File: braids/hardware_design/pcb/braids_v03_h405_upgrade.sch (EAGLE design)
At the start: 95 parts, among them IC1 74HC595D, IC2 74HC595D, IC3 LM4040B25, IC4 LM4040B10, IC5 DAC8551, IC6 LM1117-5.0, IC8 MCP6004, IC9 TL072, Q1 MMBT3904, Q2 MMBT3904, Q3 MMBT3904, Q4 MMBT3904, Q6 MMBT3904, SW1 EC12E_SW

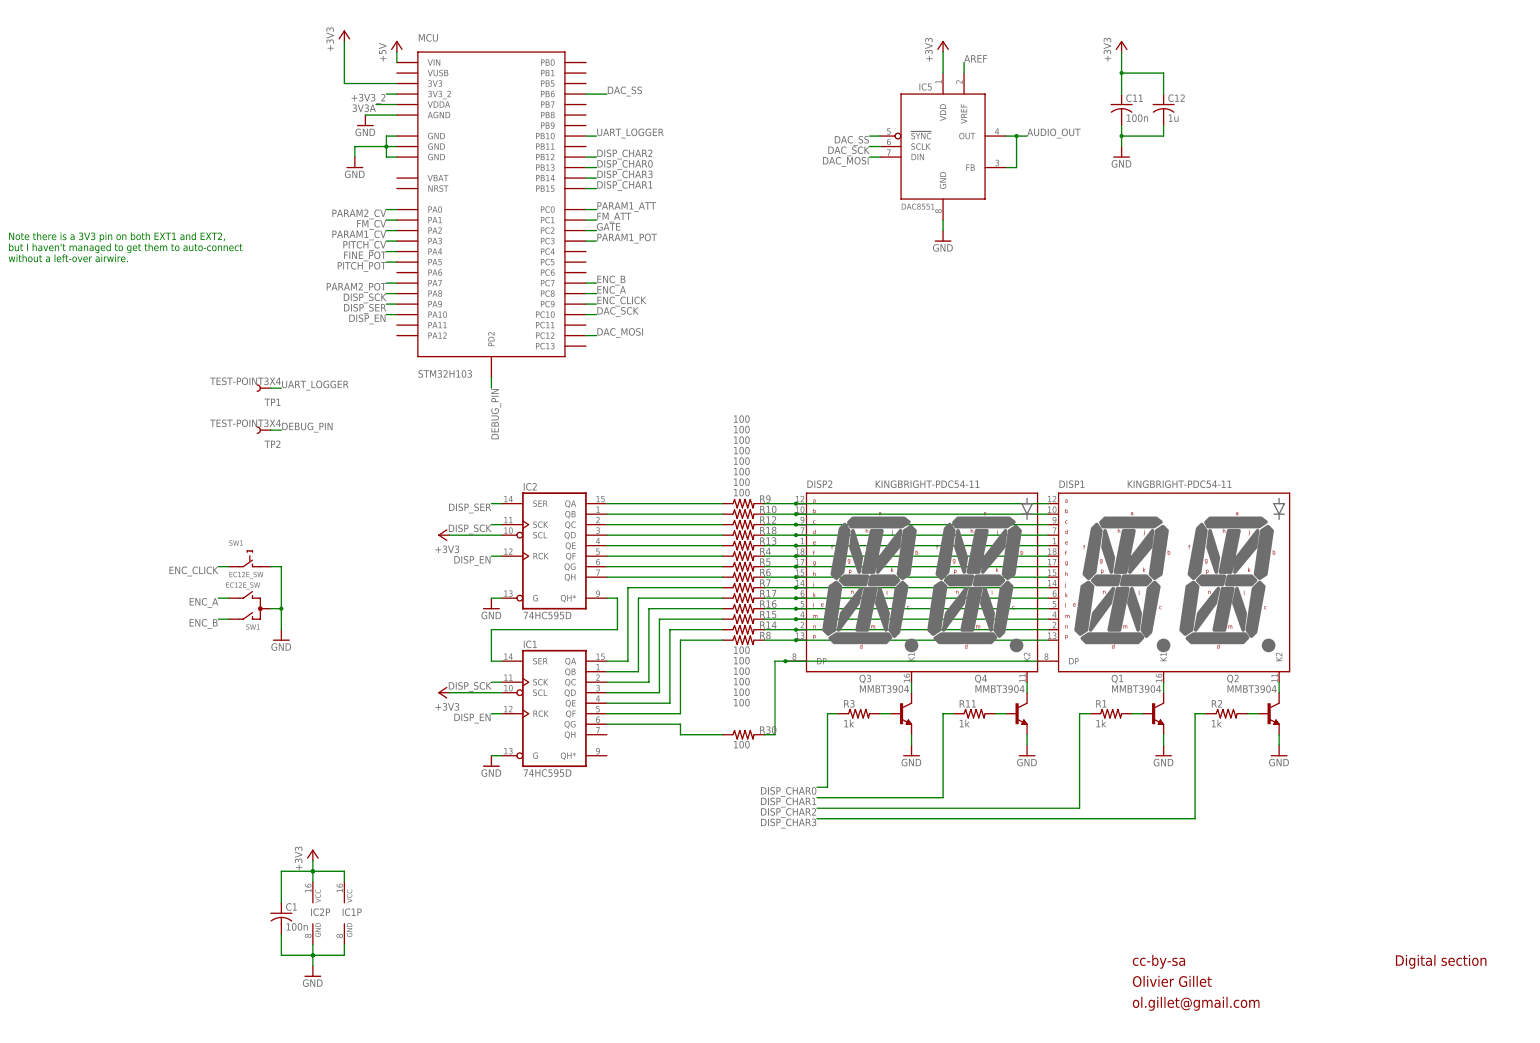
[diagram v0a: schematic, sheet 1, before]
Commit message: Add switches and LEDs, DAC uses +3V3_A
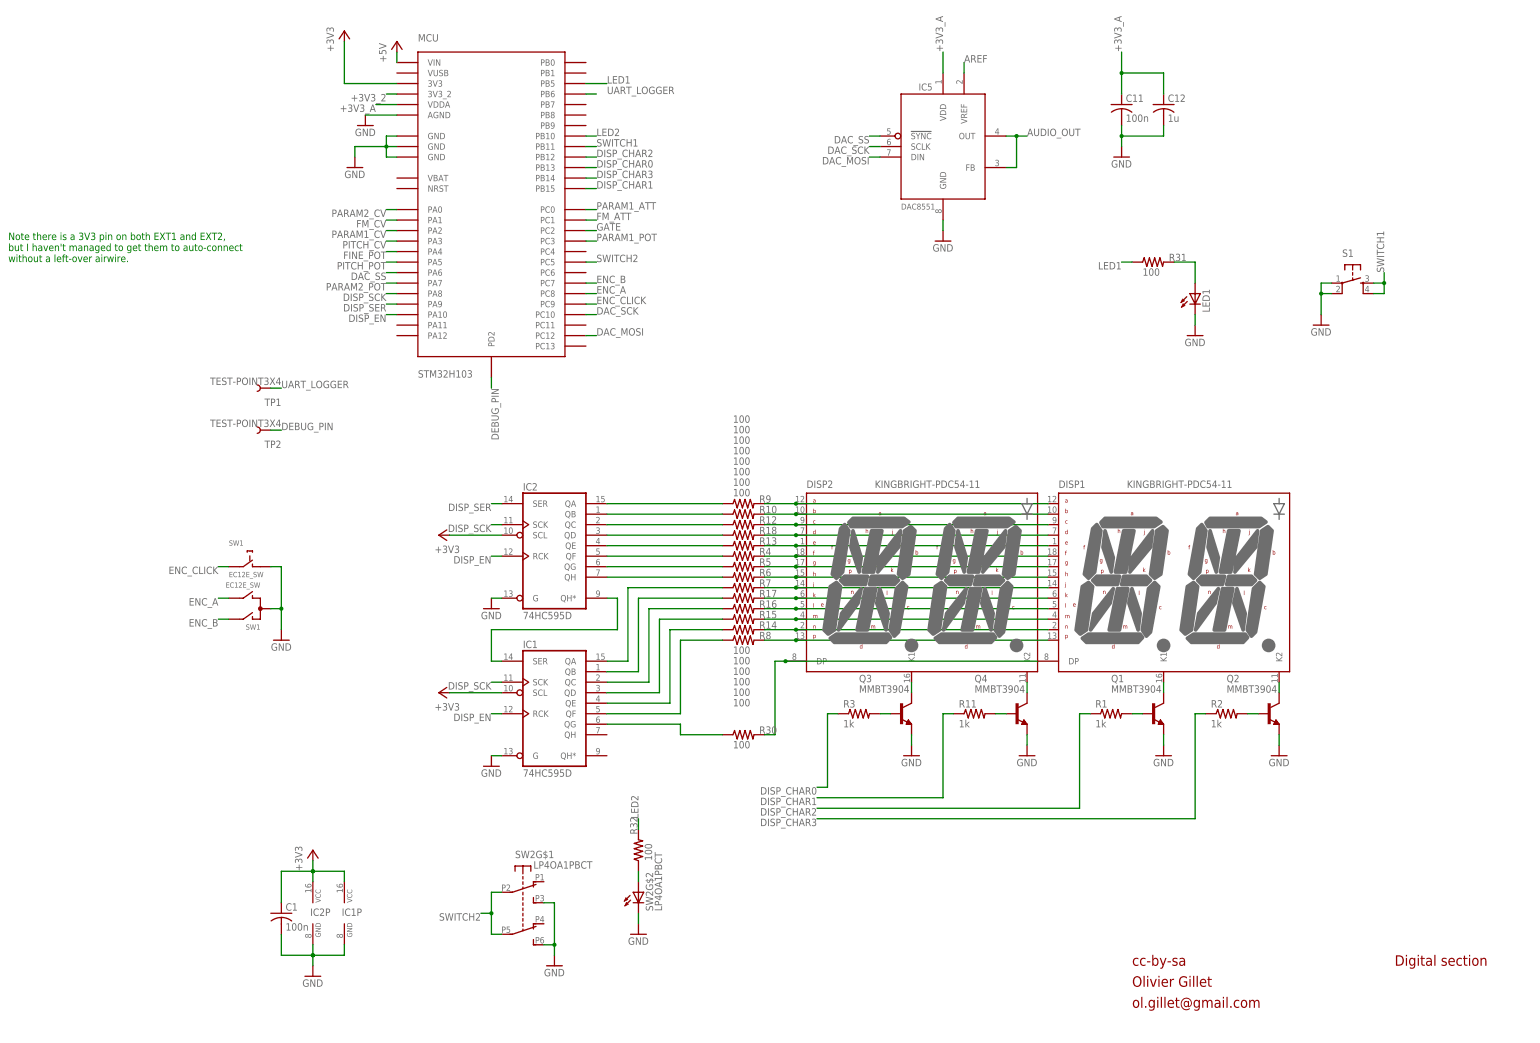
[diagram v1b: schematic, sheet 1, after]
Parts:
- added LED1: (no value), led:LED3MM
- added R31, R32: 100, rcl:R-US_R0603
- added S1: (no value), SparkFun:TAC_SWITCHPTH
- added SW2: LP4OA1PBCT, og-switch:LP4OA1PBCT
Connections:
- removed net 3V3A: C18.1, IC8P.V+, MCU.VDDA, R19.E, R20.E, R21.E, R22.1, R35.E, R36.E, R37.E
- new net +3V3_A: C11.1, C12.1, C18.1, IC5.VDD, IC8P.V+, MCU.VDDA, R19.E, R20.E, R21.E, R22.1, R35.E, R36.E, R37.E
- new net LED1: MCU.PB5, R31.1
- new net LED2: MCU.PB10, R32.2
- new net N$47: LED1.A, R31.2
- new net N$48: R32.1, SW2G$2.L1
- new net SWITCH1: MCU.PB11, S1.3, S1.4
- new net SWITCH2: MCU.PC5, SW2G$1.A2, SW2G$1.B2
- net +3V3: no longer C11.1, C12.1, IC5.VDD
- net DAC_SS: now also MCU.PA6; no longer MCU.PB6
- net GND: now also LED1.C, S1.1, S1.2, SW2G$1.A3, SW2G$1.B3, SW2G$2.L2
- net UART_LOGGER: now also MCU.PB6; no longer MCU.PB10

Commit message: Re-assign some GPIOs due to conflicts on Olimex boards, some tweaks
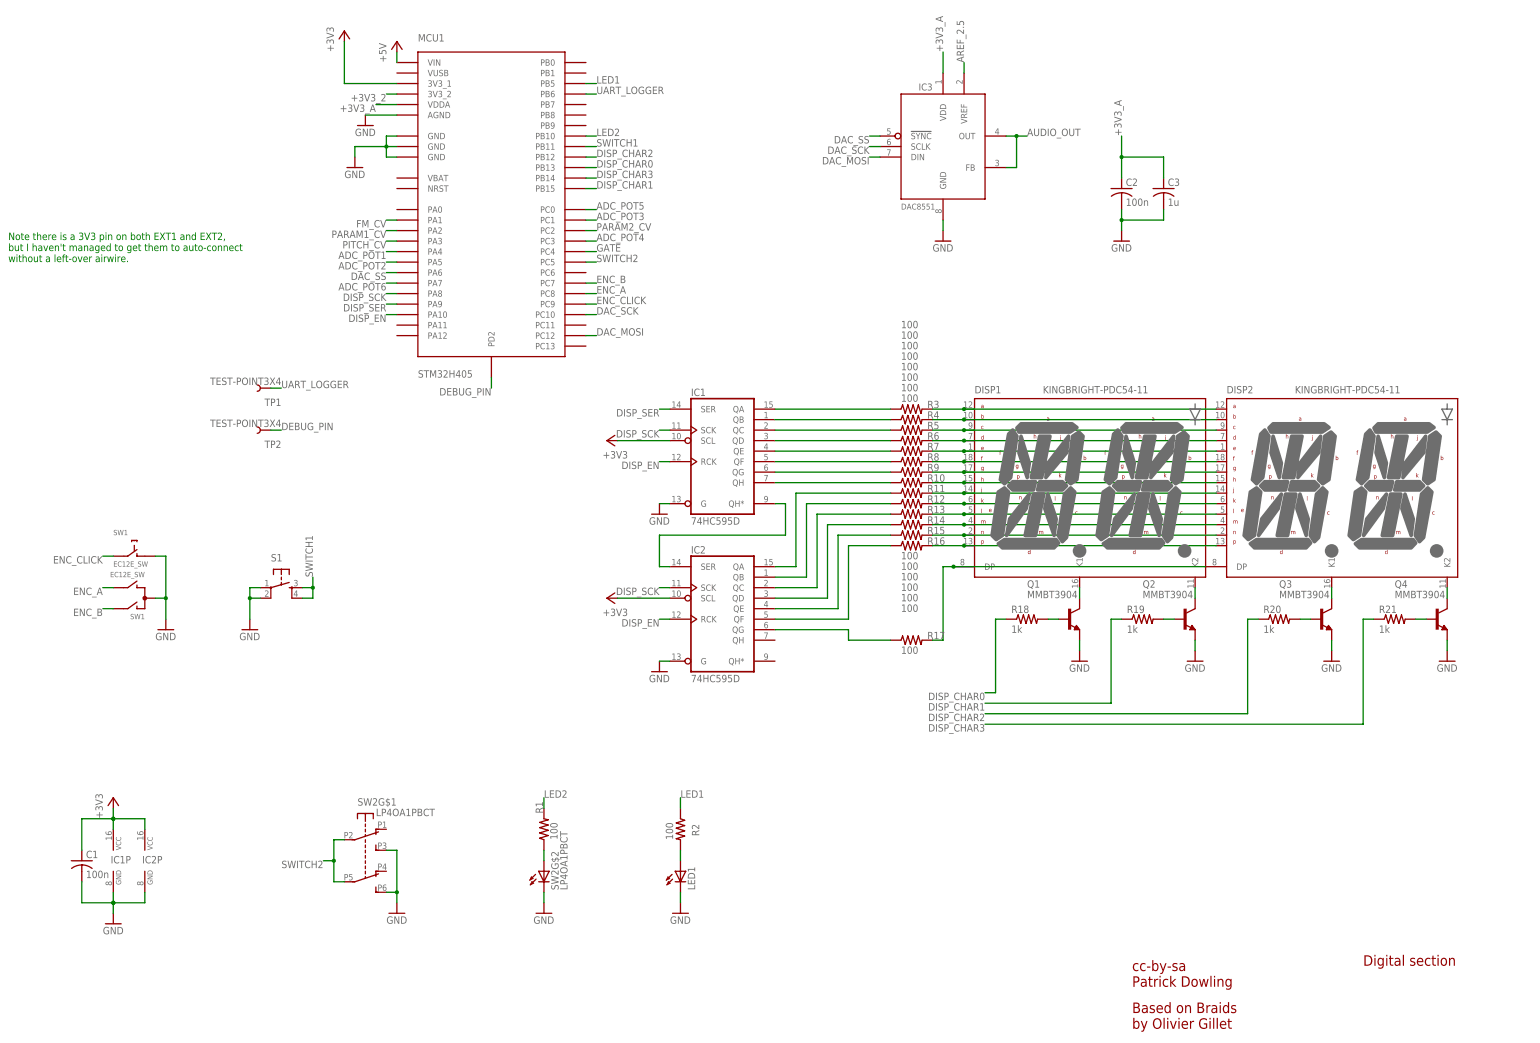
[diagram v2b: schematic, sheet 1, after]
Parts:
- removed C22, C26: 100n, rcl:C-USC0805
- removed C23: 10u, rcl:CPOL-USE2-5
- removed C24, C29: 47u, rcl:CPOL-USE2.5-7
- removed C28: 47p, rcl:C-USC0805
- removed COLOR, FM, TIMBRE, TRIG, VOCT: PJ301_THONKICONN6, og-pj301:PJ301_THONKICONN6
- removed IC9: TL072, linear:TL072D
- removed Q6: MMBT3904, transistor:MMBT3904LT1-NPN-SOT23-BEC
- removed R49: 66.5k, rcl:R-US_R0805
- removed R52, R55: 100k, rcl:R-US_R0805
- removed R53: 200k, rcl:R-US_R0805
- removed R54: 1k, rcl:R-US_R0805
- added C10, C15: 1n, rcl:C-USC0805
- added C3: 1u, rcl:C-USC0805
- added C5: 47u, rcl:CPOL-USD
- added C6, C7: 22u, rcl:CPOL-USC
- added IC7: LM4040B10, texas:LM4041B12DBZ
- added J1, J2, J3, J4, J5: PJ301_THONKICONN6, og-pj301:PJ301_THONKICONN6
- added Q5: MMBT3904, transistor:MMBT3904LT1-NPN-SOT23-BEC
- added R33: 100k, rcl:R-US_R0805
- added R34: 200k, rcl:R-US_R0805
- added R38: 33k, rcl:R-US_R0805
- added R40: 24.9k, rcl:R-US_R0805
- added R45: 10kB, pot-alps:POT_USVERTICAL_PS
- C11: device rcl:C-USC0805 -> rcl:C-USC0603
- C12: value 1u -> 470n; device rcl:C-USC0805 -> rcl:C-USC0603
- C13: value 1n -> 100n
- C14: value 22u -> 100n; device rcl:CPOL-USE2.5-6 -> rcl:C-USC0805
- C16: value 22u -> 1n; device rcl:CPOL-USE2.5-6 -> rcl:C-USC0805
- C17, C19: value 1n -> 100p
- C2: device rcl:C-USC0603 -> rcl:C-USC0805
- C20: value 100p -> 10u; device rcl:C-USC0805 -> rcl:CPOL-USE2-5
- C21: value 100p -> 47p
- C4: value 100n -> 47u; device rcl:C-USC0603 -> rcl:CPOL-USD
- C8: value 470n -> 100n
- IC3: value LM4040B25 -> DAC8551; device texas:LM4041B12DBZ -> og-dac:DAC855X
- IC4: value LM4040B10 -> LM1117-5.0; device texas:LM4041B12DBZ -> og-vreg:REG1117T
- IC5: value DAC8551 -> MCP6004; device og-dac:DAC855X -> gm-ics:TL074D
- IC6: value LM1117-5.0 -> LM4040B25; device og-vreg:REG1117T -> texas:LM4041B12DBZ
- IC8: value MCP6004 -> TL072; device gm-ics:TL074D -> linear:TL072D
- MCU1: value STM32H103 -> STM32H405
- R1, R11, R2, R3: value 1k -> 100
- R18: value 100 -> 1k
- R19, R20, R21: value 10kB -> 1k; device pot-alps:POT_USVERTICAL_PS -> rcl:R-US_R0603
- R22: value 150 -> 100k; device rcl:R-US_R0603 -> rcl:R-US_R0805
- R23: value 100k -> 10k
- R27: value 10k -> 100k
- R28: value 100k -> 33k
- R29: value 470 -> 33k; device rcl:R-US_R0603 -> rcl:R-US_R0805
- R30: value 100 -> 150
- R31: value 100 -> 470
- R32: value 100 -> 100k; device rcl:R-US_R0603 -> rcl:R-US_R0805
- R35: value 10kB -> 100k; device pot-alps:POT_USVERTICAL_PS -> rcl:R-US_R0805
- R36: value 10kB -> 39k; device pot-alps:POT_USVERTICAL_PS -> rcl:R-US_R0805
- R37: value 10kB -> 33k; device pot-alps:POT_USVERTICAL_PS -> rcl:R-US_R0805
- R39: value 33k -> 39k
- R41: value 33k -> 10kB; device rcl:R-US_R0805 -> pot-alps:POT_USVERTICAL_PS
- R42: value 39k -> 10kB; device rcl:R-US_R0805 -> pot-alps:POT_USVERTICAL_PS
- R43: value 39k -> 100k
- R44: value 100k -> 1k
- R46: value 100k -> 10kB; device rcl:R-US_R0805 -> pot-alps:POT_USVERTICAL_PS
- R47: value 24.9k -> 10kB; device rcl:R-US_R0805 -> pot-alps:POT_USVERTICAL_PS
- R48: value 66.5k -> 10kB; device rcl:R-US_R0805 -> pot-alps:POT_USVERTICAL_PS
- renumbered AUDIO to J6, C25 to C9, D3 to D2, JP2 to JP1, MCU to MCU1
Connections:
- removed net AREF: C8.1, IC3.C, IC5.VREF, R22.2
- removed net FINE_POT: MCU1.PA4, R19.S
- removed net FM_ATT: MCU1.PC1, R21.S
- removed net N$11: R44.1, VOCT.3
- removed net N$12: FM.3, R46.1
- removed net N$37 (its old number): IC2A.QF, R4.1
- removed net N$7: COLOR.3, R52.1
- removed net N$8: R23.1, TIMBRE.3
- removed net PARAM1_ATT: MCU1.PC0, R36.S
- removed net PARAM1_POT: MCU1.PC3, R35.S
- removed net PARAM2_POT: MCU1.PA7, R37.S
- removed net PITCH_POT: MCU1.PA5, R20.S
- new net ADC_POT1: MCU1.PA4, R41.S
- new net ADC_POT2: MCU1.PA5, R45.S
- new net ADC_POT3: MCU1.PC1, R47.S
- new net ADC_POT4: MCU1.PC3, R42.S
- new net ADC_POT5: MCU1.PC0, R46.S
- new net ADC_POT6: MCU1.PA7, R48.S
- new net AREF_2.5: C12.1, IC3.VREF, IC6.C, R30.2
- new net COLOR: J5.3, R25.1
- new net FM: J3.3, R35.1
- new net N$44: IC2A.QF, R16.1
- new net TIMBRE: J4.3, R27.1
- new net VOCT: J2.3, R33.1
- net +3V3: now also MCU1.3V3_1; no longer MCU1.3V3
- net +3V3_2: now also R23.2; no longer R27.2
- net +3V3_A: now also C2.1, C3.1, IC3.VDD, IC5P.V+, R30.1, R41.E, R42.E, R45.E, R46.E, R47.E, R48.E; no longer C11.1, C12.1, IC5.VDD, IC8P.V+, R19.E, R20.E, R21.E, R22.1, R35.E, R36.E, R37.E
- net +5V: now also C7.+, C8.1, IC4.VOUT; no longer C14.+, C4.1, IC6.VOUT
- net AREF_-10: now also C11.1, IC7.A, R31.2, R32.1, R34.1; no longer C2.1, IC4.A, R25.1, R29.2, R53.1
- net AUDIO_OUT: now also IC3.FB, IC3.OUT, R36.2; no longer IC5.FB, IC5.OUT, R42.2
- net DAC_MOSI: now also IC3.DIN; no longer IC5.DIN
- net DAC_SCK: now also IC3.SCLK; no longer IC5.SCLK
- net DAC_SS: now also IC3.!SYNC; no longer IC5.!SYNC
- net DISP_CHAR0: now also R18.1; no longer R3.1
- net DISP_CHAR1: now also R19.1; no longer R11.1
- net DISP_CHAR2: now also R20.1; no longer R1.1
- net DISP_CHAR3: now also R21.1; no longer R2.1
- net DISP_SER: now also IC1A.SER; no longer IC2A.SER
- net FM_CV: now also C15.2, IC5D.OUT, R37.2; no longer C13.2, IC8D.OUT, R39.2
- net GATE: now also MCU1.PC4, Q5.C, R23.1; no longer MCU1.PC2, Q6.C, R27.1
- net GATE_IN: now also Q5.B, R22.2; no longer Q6.B, R28.2
- net GND: now also C13.2, C14.1, C17.2, C3.2, C4.-, C5.+, C6.-, C7.-, IC3.GND, IC4.GND, IC5A.+IN, IC5B.+IN, IC5C.+IN, IC5D.+IN, IC5P.V-, IC6.A, IC7.C, J1.1, J1.2, J2.1, J3.1, J4.1, J5.1, Q5.E, R41.A, R42.A, R45.A, R46.A, R47.A, R48.A; no longer C14.-, C16.-, C21.2, C22.2, C24.-, C26.1, C29.+, C4.2, COLOR.1, FM.1, IC3.A, IC4.C, IC5.GND, IC6.GND, IC8B.+IN, IC8C.+IN, IC8D.+IN, IC8P.V-, IC9A.+IN, Q6.E, R19.A, R20.A, R21.A, R35.A, R36.A, R37.A, TIMBRE.1, TRIG.1, TRIG.2, VOCT.1
- net LED1: now also R2.1; no longer R31.1
- net LED2: now also R1.2; no longer R32.2
- net N$10: now also Q4.B, R21.2; no longer Q2.B, R2.2
- net N$15: now also R3.2; no longer R9.2
- net N$16: now also R4.2; no longer R10.2
- net N$17: now also R5.2; no longer R12.2
- net N$18: now also R6.2; no longer R18.2
- net N$19: now also R7.2; no longer R13.2
- net N$20: now also R8.2; no longer R4.2
- net N$21: now also R9.2; no longer R5.2
- net N$22: now also R10.2; no longer R6.2
- net N$23: now also R11.2; no longer R7.2
- net N$24: now also R12.2; no longer R17.2
- net N$25: now also R13.2; no longer R16.2
- net N$26: now also R14.2; no longer R15.2
- net N$27: now also R15.2; no longer R14.2
- net N$28: now also R16.2; no longer R8.2
- net N$29: now also R17.2; no longer R30.2
- net N$30: now also IC1A.QH, R10.1; no longer IC2A.QH, R6.1
- net N$31: now also IC1A.QH*, IC2A.SER; no longer IC1A.SER, IC2A.QH*
- net N$32: now also IC1A.QA, R3.1; no longer IC2A.QA, R9.1
- net N$33: now also IC1A.QB, R4.1; no longer IC2A.QB, R10.1
- net N$34: now also IC1A.QC, R5.1; no longer IC2A.QC, R12.1
- net N$35: now also IC1A.QD, R6.1; no longer IC2A.QD, R18.1
- net N$36: now also IC1A.QE, R7.1; no longer IC2A.QE, R13.1
- net N$38: now also IC1A.QG, R9.1; no longer IC2A.QG, R5.1
- net N$39: now also IC2A.QA, R11.1; no longer IC1A.QA, R7.1
- net N$40: now also IC2A.QB, R12.1; no longer IC1A.QB, R17.1
- net N$41: now also IC2A.QC, R13.1; no longer IC1A.QC, R16.1
- net N$42: now also IC2A.QD, R14.1; no longer IC1A.QD, R15.1
- net N$43: now also IC2A.QE, R15.1; no longer IC1A.QE, R14.1
- net N$45: now also IC5B.-IN, R24.2, R25.2, R28.1; no longer IC8B.-IN, R48.1, R52.2, R53.2
- net N$46: now also IC2A.QG, R17.1; no longer IC1A.QG, R30.1
- net N$47: now also R2.2; no longer R31.2
- net N$48: now also R1.1; no longer R32.1
- net N$5: now also Q1.B, R18.2; no longer Q3.B, R3.2
- net N$50: now also C15.1, IC5D.-IN, R34.2, R35.2, R37.1; no longer C13.1, IC8D.-IN, R26.2, R39.1, R46.2
- net N$52: now also C10.1, IC5A.-IN, R26.2, R27.2, R29.1; no longer C17.1, IC8A.-IN, R23.2, R24.2, R49.1
- net N$57: now also J1.3, R22.1; no longer R28.1, TRIG.3
- net N$6: now also Q2.B, R19.2; no longer Q4.B, R11.2
- net N$63: now also C16.1, IC5C.-IN, R32.2, R33.2, R38.1; no longer C19.1, IC8C.-IN, R25.2, R41.1, R44.2
- net N$67: now also C19.2, C20.+, IC8B.-IN, IC8B.OUT; no longer C20.2, C23.+, IC9B.-IN, IC9B.OUT
- net N$68: now also C20.-, R40.2; no longer C23.-, R47.2
- net N$69: now also C17.1, IC8B.+IN, R39.1; no longer C21.1, IC9B.+IN, R43.1
- net N$71: now also C19.1, R36.1, R39.2; no longer C20.1, R42.1, R43.2
- net N$72: now also R43.1, R44.1; no longer R54.1, R55.1
- net N$73: now also C21.2, IC8A.OUT, R44.2; no longer C28.2, IC9A.OUT, R54.2
- net N$75: now also C21.1, IC8A.-IN, R40.1, R43.2; no longer C28.1, IC9A.-IN, R47.1, R55.2
- net N$9: now also Q3.B, R20.2; no longer Q1.B, R1.2
- net PARAM1_CV: now also C10.2, IC5A.OUT, R29.2; no longer C17.2, IC8A.OUT, R49.2
- net PARAM2_CV: now also IC5B.OUT, MCU1.PC2, R28.2; no longer IC8B.OUT, MCU1.PA0, R48.2
- net PITCH_CV: now also C16.2, IC5C.OUT, R38.2; no longer C19.2, IC8C.OUT, R41.2
- net VCC: now also C13.1, C4.+, C6.+, IC4.VIN, IC8P.V+; no longer C16.+, C22.1, C24.+, IC6.VIN, IC9P.V+
- net VEE: now also C14.2, C5.-, IC8P.V-, R31.1; no longer C26.2, C29.-, IC9P.V-, R29.1
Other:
- note added: "(12-10=2v)/470=4mA 100uA <= 4mA < 15mA load: opamp input current 470/100n = LP 3.3KHz?"
- note added: "(3.3-2.5v=2v)/150=5mA ~73uA <= 5mA < 15mA DAC8551 ref current 20uA? 150/470n = LP 2.2KHz?"
- note added: "Based on Braids by Olivier Gillet"
- note added: "COLOR"
- note added: "FINE"
- note added: "FM"
- note added: "MODULATION"
- note added: "PITCH"
- note added: "TIMBRE"
- note added: "TL072"
- note added: "cc-by-sa Patrick Dowling"
- note removed: "0.0 to 5.0v"
- note removed: "Olivier Gillet"
- note removed: "cc-by-sa"
- note removed: "ol.gillet@gmail.com"
- moved on the sheet: C1, C13, C17, C18, C19, C21, C8, DISP1, DISP2, IC1, IC1P, IC2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

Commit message: Yet another GPIO re-assign...
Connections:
- net GATE: now also MCU1.PC2; no longer MCU1.PC4
- net PARAM2_CV: now also MCU1.PB1; no longer MCU1.PC2
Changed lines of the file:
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@@
 <net name="PARAM2_CV" class="0">
+<segment>
+<pinref part="MCU1" gate="G$1" pin="PB1"/>
+<wire x1="-45.72" y1="139.7" x2="-43.18" y2="139.7" width="0.1524" layer="91"/>
+<label x="-43.18" y="139.7" size="1.778" layer="95"/>
+</segment>
+</net>
+<net name="GATE" class="0">
 <segment>
 <pinref part="MCU1" gate="G$1" pin="PC2"/>
@@
 </segment>
 </net>
-<net name="GATE" class="0">
-<segment>
-<pinref part="MCU1" gate="G$1" pin="PC4"/>
-<wire x1="-45.72" y1="96.52" x2="-43.18" y2="96.52" width="0.1524" layer="91"/>
-<label x="-43.18" y="96.52" size="1.778" layer="95"/>
-</segment>
-</net>

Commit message: Board tweaks
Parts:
- added R49: 100k, rcl:R-US_R1206
- C11, C12, C8: device rcl:C-USC0603 -> rcl:C-USC0805
- R1, R30, R31: device rcl:R-US_R0603 -> rcl:R-US_R0805
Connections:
- new net N$7: C6.+, IC4.VIN, R49.1
- net VCC: now also R49.2; no longer C6.+, IC4.VIN
